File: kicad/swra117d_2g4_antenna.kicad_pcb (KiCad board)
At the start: 2 copper layers, 40 x 30 mm, 2 parts, among them J1 SMA edge launch

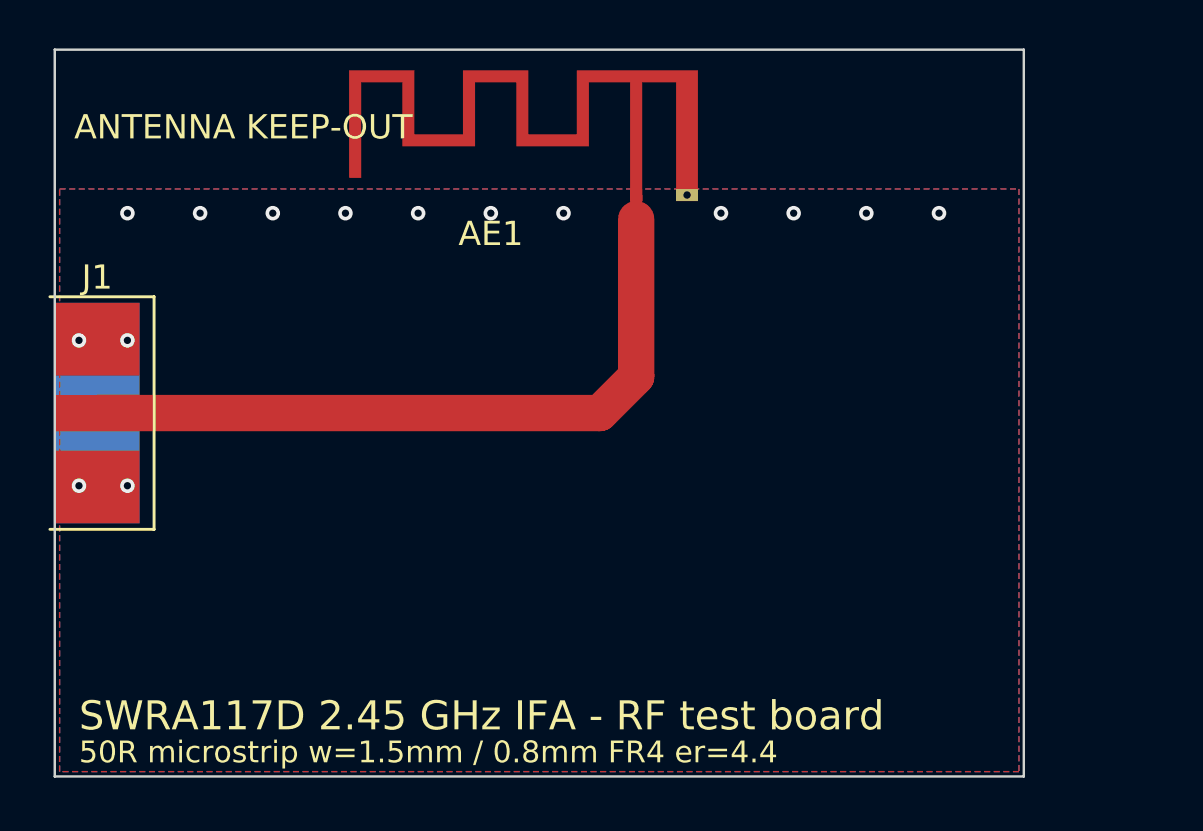
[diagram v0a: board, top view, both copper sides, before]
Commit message: Put the SMA below the antenna feed: one straight 24 mm 50 ohm run
The connector moves to the bottom edge at x = 124, rotated to face the
antenna's feed pad directly, so the feed is a single vertical run of 24.0 mm
with no corner - down from 32.1 mm through a 20 mm horizontal detour and a
45 degree bend. That is the shortest an edge launch can be on this board:
the antenna owns the top edge, its ground pin blocks any approach from the
right, and the connector needs 9.1 mm of board edge entirely on the ground
plane, which only the bottom edge offers. BOARD_H is now a constant, so 26
or 22 mm boards (18.3 / 14.3 mm feeds) are one edit - at the cost of the
ground plane, which is the antenna's counterpoise.

The pour keep-away is now one corridor following the line, and 8 ground
vias sit inside the connector's own pads so the coplanar ground at the
launch is tied to the bottom plane right there.

openEMS no longer assumes an x-directed launch: it takes the axis and
direction from the first track segment and places the port on whichever
board edge the line starts from. The ngspice deck follows the new length
(TD 146 ps, 129 degrees at 2.45 GHz instead of 195 ps / 172 degrees).

README gains a section on what this cannot do: for a lossless matched line
|gamma| at the connector equals |gamma| at the antenna, so the VSWR curve
and the frequency of its dip are line-invariant. A shorter feed buys a
readable Smith chart and a little less loss, not a moved resonance.

Co-Authored-By: Claude Opus 5 <noreply@anthropic.com>
Claude-Session: https://claude.ai/code/session_01Prj6bUQ2KQzzxzD4bgtswJ
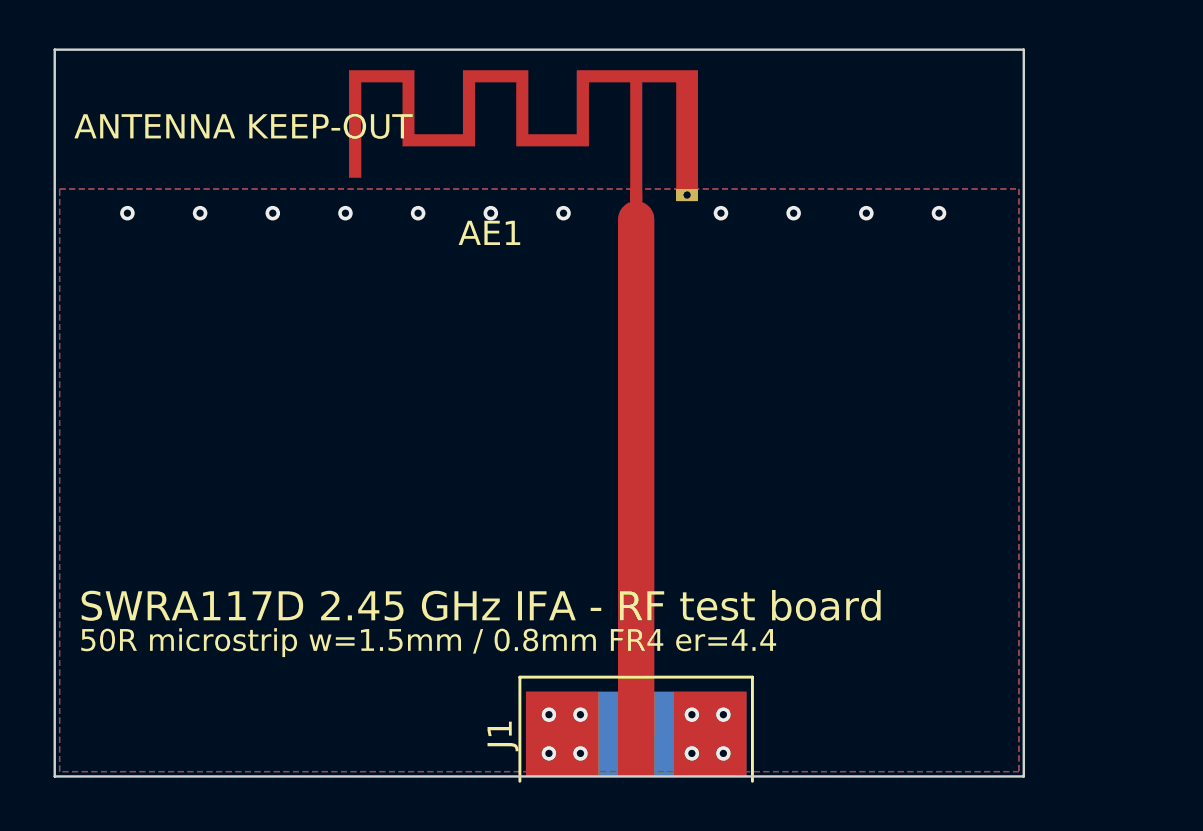
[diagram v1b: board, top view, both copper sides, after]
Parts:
- moved J1 28.3 mm to (124.0, 90.0), turned to 90 degrees
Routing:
- net ANT_FEED: track 30.4 -> 22.2 mm
- net GND: vias 15 -> 19
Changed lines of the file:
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@@
 	(footprint "SWRA117D_RF:SMA_EdgeMount_Generic"
 		(layer "F.Cu")
-		(at 100 75)
+		(at 124 90 90)
 		(descr "Generic end-launch (edge-mount) SMA jack for a 0.8 mm two layer board. Origin sits on the board edge: the signal pad starts at x = 0 and the connector body hangs off the outside of the Edge.Cuts line. Pad 1 = signal, pad 2 = shell ground: two tabs either side of the signal pad on the top, one solid plane under the whole launch on the bottom, so the launch keeps its reference without relying on a zone fill."
 		)
@@
 		(attr smd)
 		(property "Reference" "J1"
-			(at 1.75 -5.6 0)
+			(at 1.75 -5.6 90)
 			(layer "F.SilkS")
 			(effects (font (size 1 1) (thickness 0.15)))
@@
 		)
 		(property "Value" "SMA edge launch"
-			(at 1.75 5.6 0)
+			(at 1.75 5.6 90)
 			(layer "F.Fab")
 			(effects (font (size 1 1) (thickness 0.15)))
@@
 		)
 		(fp_text user "%R"
-			(at 1.75 0 0)
+			(at 1.75 0 90)
 			(layer "F.Fab")
 			(effects (font (size 0.8 0.8) (thickness 0.12)))
@@
 		)
 		(pad "1" smd rect
-			(at 1.75 0)
+			(at 1.75 0 90)
 			(size 3.5 1.5)
 			(layers "F.Cu" "F.Paste" "F.Mask")
@@
 		)
 		(pad "2" smd rect
-			(at 1.75 -3.05)
+			(at 1.75 -3.05 90)
 			(size 3.5 3)
 			(layers "F.Cu" "F.Paste" "F.Mask")
@@
 		)
 		(pad "2" smd rect
-			(at 1.75 3.05)
+			(at 1.75 3.05 90)
 			(size 3.5 3)
 			(layers "F.Cu" "F.Paste" "F.Mask")
@@
 		)
 		(pad "2" smd rect
-			(at 1.75 0)
+			(at 1.75 0 90)
 			(size 3.5 9.1)
 			(layers "B.Cu" "B.Paste" "B.Mask")
@@
 	)
 	(gr_text "SWRA117D 2.45 GHz IFA - RF test board"
-		(at 101 87.5 0)
+		(at 101 83 0)
 		(layer "F.SilkS")
 		(effects (font (size 1.2 1.2) (thickness 0.15)) (justify left))
 	)
 	(gr_text "50R microstrip w=1.5mm / 0.8mm FR4 er=4.4"
-		(at 101 89 0)
+		(at 101 84.4 0)
 		(layer "F.SilkS")
 		(effects (font (size 0.9 0.9) (thickness 0.15)) (justify left))
 	)
 	(segment
-		(start 101.75 75)
-		(end 122.5 75)
-		(width 1.5)
-		(layer "F.Cu")
-		(net 2)
-	)
-	(segment
-		(start 122.5 75)
-		(end 124 73.5)
-		(width 1.5)
-		(layer "F.Cu")
-		(net 2)
-	)
-	(segment
-		(start 124 73.5)
+		(start 124 88.25)
 		(end 124 67)
 		(width 1.5)
@@
 	)
 	(via
-		(at 101 72)
-		(size 0.6)
-		(drill 0.3)
-		(layers "F.Cu" "B.Cu")
-		(net 1)
-	)
-	(via
-		(at 103 72)
-		(size 0.6)
-		(drill 0.3)
-		(layers "F.Cu" "B.Cu")
-		(net 1)
-	)
-	(via
-		(at 101 78)
-		(size 0.6)
-		(drill 0.3)
-		(layers "F.Cu" "B.Cu")
-		(net 1)
-	)
-	(via
-		(at 103 78)
+		(at 120.4 87.45)
+		(size 0.6)
+		(drill 0.3)
+		(layers "F.Cu" "B.Cu")
+		(net 1)
+	)
+	(via
+		(at 120.4 89.05)
+		(size 0.6)
+		(drill 0.3)
+		(layers "F.Cu" "B.Cu")
+		(net 1)
+	)
+	(via
+		(at 121.7 87.45)
+		(size 0.6)
+		(drill 0.3)
+		(layers "F.Cu" "B.Cu")
+		(net 1)
+	)
+	(via
+		(at 121.7 89.05)
+		(size 0.6)
+		(drill 0.3)
+		(layers "F.Cu" "B.Cu")
+		(net 1)
+	)
+	(via
+		(at 126.3 87.45)
+		(size 0.6)
+		(drill 0.3)
+		(layers "F.Cu" "B.Cu")
+		(net 1)
+	)
+	(via
+		(at 126.3 89.05)
+		(size 0.6)
+		(drill 0.3)
+		(layers "F.Cu" "B.Cu")
+		(net 1)
+	)
+	(via
+		(at 127.6 87.45)
+		(size 0.6)
+		(drill 0.3)
+		(layers "F.Cu" "B.Cu")
+		(net 1)
+	)
+	(via
+		(at 127.6 89.05)
 		(size 0.6)
 		(drill 0.3)
@@
 		(net_name "")
 		(layers "F.Cu")
-		(name "RF_POUR_KEEPAWAY_H")
+		(name "RF_POUR_KEEPAWAY")
 		(hatch full 0.508)
 		(connect_pads (clearance 0))
@@
 		)
 		(fill (thermal_gap 0.4) (thermal_bridge_width 0.4))
-		(polygon (pts (xy 99.5 73.25) (xy 125.75 73.25) (xy 125.75 76.75) (xy 99.5 76.75)))
-	)
-	(zone
-		(net 0)
-		(net_name "")
-		(layers "F.Cu")
-		(name "RF_POUR_KEEPAWAY_V")
-		(hatch full 0.508)
-		(connect_pads (clearance 0))
-		(min_thickness 0.25)
-		(filled_areas_thickness no)
-		(keepout
-			(tracks allowed)
-			(vias allowed)
-			(pads allowed)
-			(copperpour not_allowed)
-			(footprints allowed)
-		)
-		(fill (thermal_gap 0.4) (thermal_bridge_width 0.4))
-		(polygon (pts (xy 122.25 65.75) (xy 125.75 65.75) (xy 125.75 76.75) (xy 122.25 76.75)))
+		(polygon (pts (xy 122.25 65.75) (xy 125.75 65.75) (xy 125.75 90.5) (xy 122.25 90.5)))
 	)
 	(embedded_fonts no)

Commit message: Retune the antenna by uniform scaling: x1.155 for the 2.83 GHz result
RFsim put this board's resonance at 2.83 GHz, 15% above the ISM band, so
the board now carries a x1.155 scaled radiator generated by the new
tools/scale_footprint.py. The published footprint stays in the library
untouched, to re-scale from.

Uniform in-plane scaling is the retune that needs no model of the meander:
scale every dimension and every gap by k and each current path and coupling
distance scales with it, so resonance moves as 1/k, k = 2.83/2.45. Scaling
also carries the feed tap and the short with it, so the input impedance is
preserved - lengthening one arm by hand would fix the frequency and break
the 50 ohm. It is first order (the substrate does not scale), so expect one
more iteration: simulate, take the ratio, rescale. ANT_SCALE and
ANT_FOOTPRINT are single constants in gen_project.py.

Supporting changes: the ground plane edge is now read from the antenna
footprint's own Dwgs.User keep-out box instead of being hardcoded, so a
rescaled antenna moves the plane with it; ANT_ORIGIN drops 0.5 mm to keep
the larger antenna clear of the board edge; the feed is 23.5 mm (TD 143 ps)
and the ngspice deck follows; the symbol points at the footprint the board
uses.

Recorded in the README what could not be established analytically: a
quarter-wave check on the arm (21.31 mm2 of copper at 0.5 mm wide -> 42.6 mm
developed, ~32.8 mm arm) needs eps_eff = 0.87 to land on 2.45 GHz and 0.65
for 2.83 GHz, both below 1. The developed length badly over-predicts the
electrical length because a meander's adjacent segments carry opposing
currents, so this geometry's resonance can only come from a field solver or
a VNA - which is why the retune uses the ratio of two frequencies rather
than a model of either.

Co-Authored-By: Claude Opus 5 <noreply@anthropic.com>
Claude-Session: https://claude.ai/code/session_01Prj6bUQ2KQzzxzD4bgtswJ
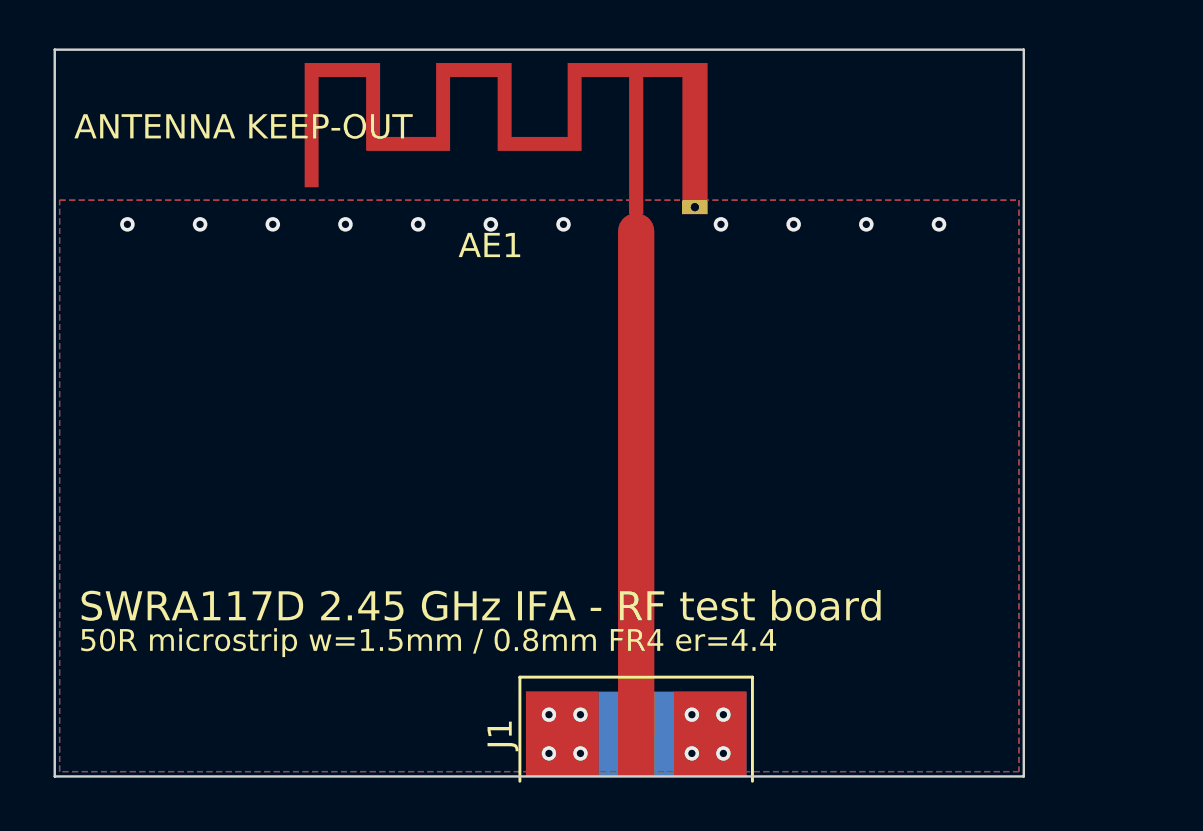
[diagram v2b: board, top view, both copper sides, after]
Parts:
- AE1: footprint SWRA117D_RF:Texas_SWRA117D_2.4GHz_Left -> SWRA117D_RF:SWRA117D_2G4_Left_retuned
- moved AE1 0.50 mm to (124.0, 66.5)
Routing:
- net ANT_FEED: track 22.2 -> 21.8 mm
